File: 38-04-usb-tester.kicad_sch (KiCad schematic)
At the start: 64 parts, among them J1 USB3_A_HC-USB3.0-L168-WP, J2 USB_Micro-B_KH-MICRO5P-JN, J3 USB_C_12401832E402A, J4 USB_Mini-B_U-M-M5DD-W-1, J5 Conn_01x05_Pin, J6 USB_C_12401832E402A, SW1 SW_SPDT, U1 STM32C031K6Tx

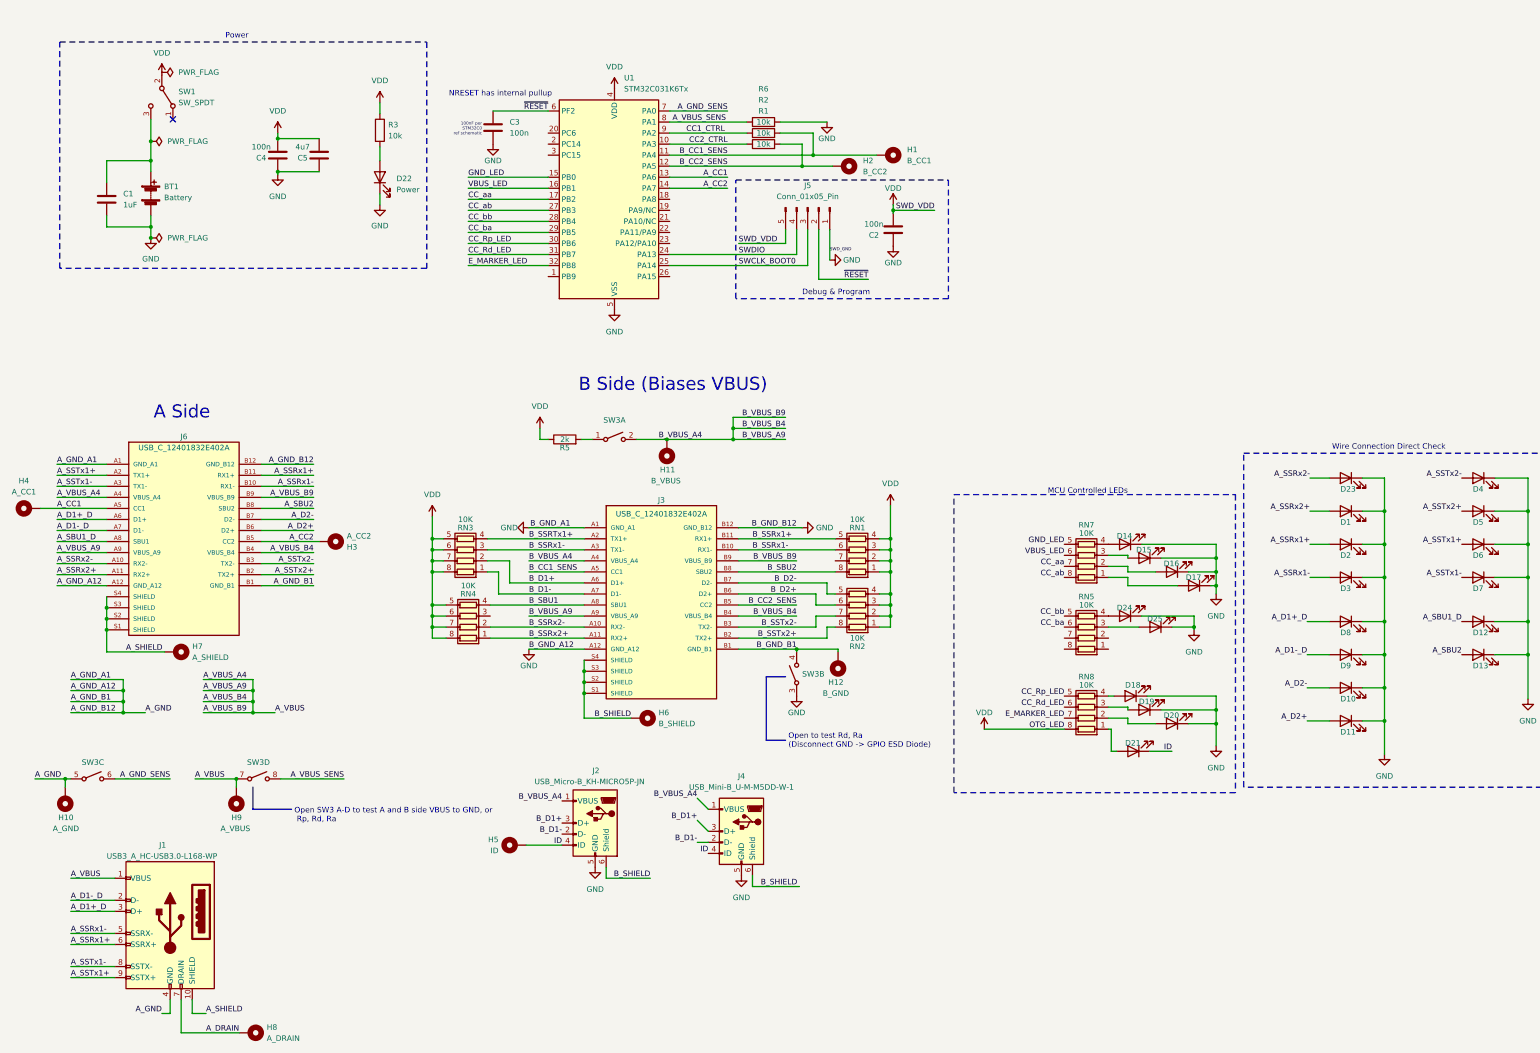
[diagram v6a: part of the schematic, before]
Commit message: edge pads and start of pcb layout
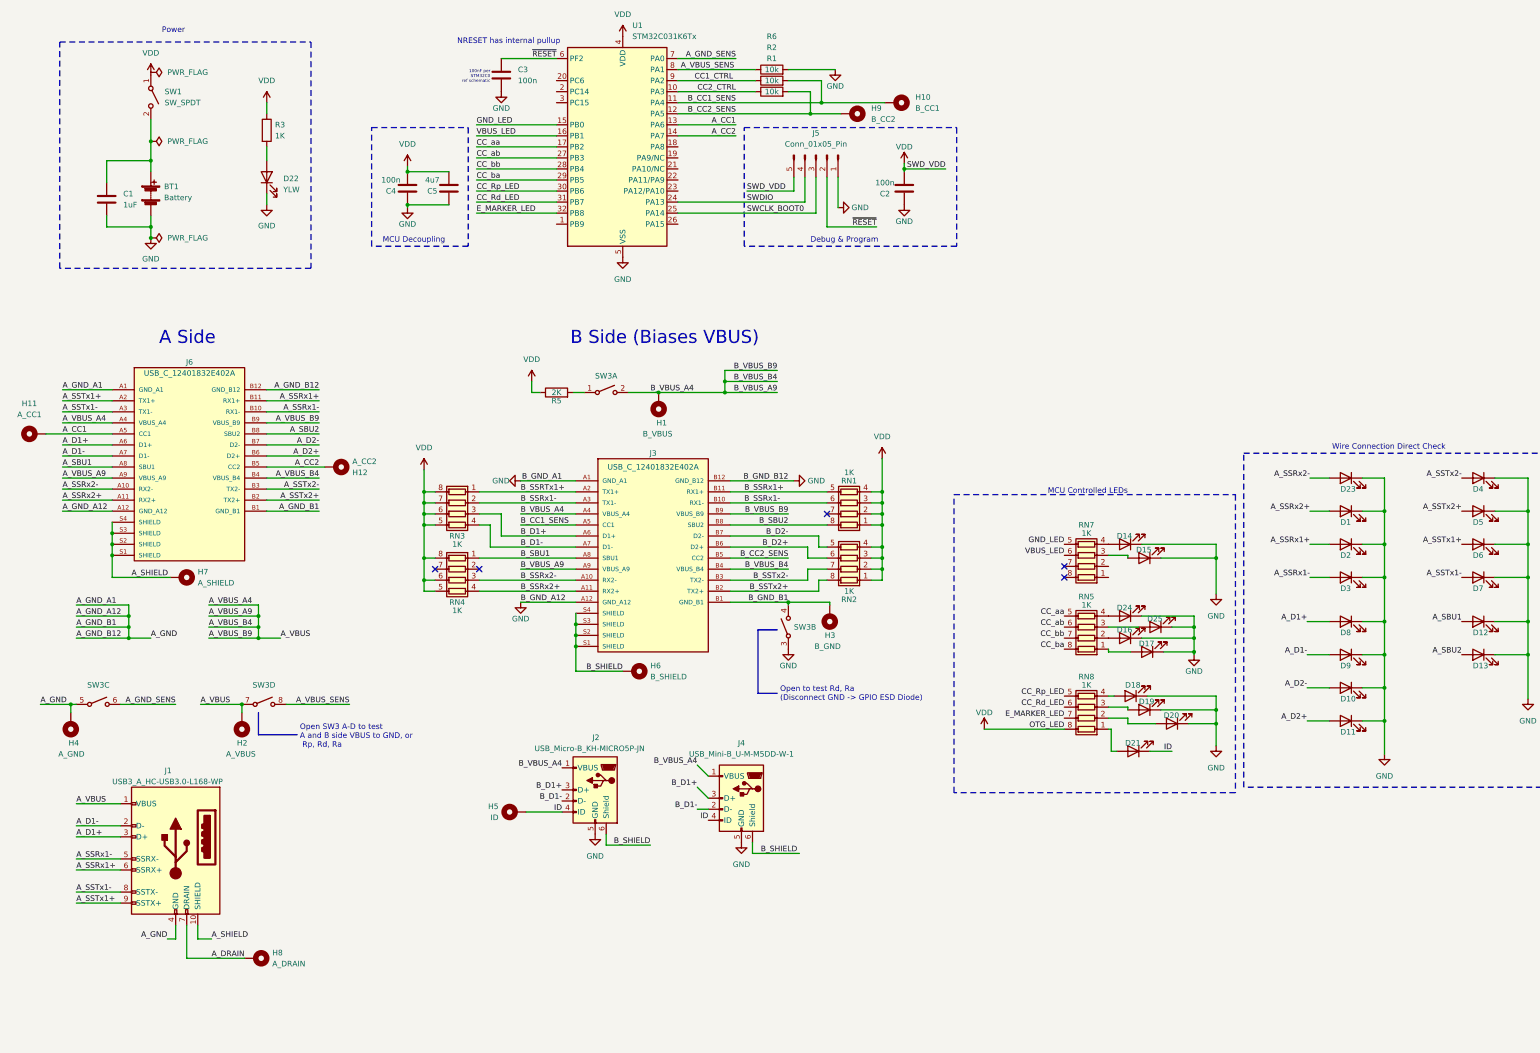
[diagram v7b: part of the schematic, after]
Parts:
- BT1: footprint Battery:BatteryHolder_Keystone_1058_1x2032 -> Battery:BatteryHolder_Keystone_103_1x20mm
- C1, C2, C3, C4, C5: footprint Capacitor_SMD:C_0805_2012Metric -> Capacitor_SMD:C_0603_1608Metric
- D1, D13, D9: value SSRx2+_D -> YLW; JLPCB_MPN (none) -> 17-21UYC/S530-A3/TR8; JLPCB_Mfg (none) -> Everlight Elec; JLPCB_Part_No (none) -> C91839; JLPCB_Price (none) -> $0.0218; JLPCB_URL (none) -> https://jlcpcb.com/parts/2nd/Optocoupler_LED_Digital_Tube_P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
- D10, D2: value SSRx1+_D -> YLW; JLPCB_MPN (none) -> 17-21UYC/S530-A3/TR8; JLPCB_Mfg (none) -> Everlight Elec; JLPCB_Part_No (none) -> C91839; JLPCB_Price (none) -> $0.0218; JLPCB_URL (none) -> https://jlcpcb.com/parts/2nd/Optocoupler_LED_Digital_Tube_P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
- D11, D3: value SSRx1-_D -> YLW; JLPCB_MPN (none) -> 17-21UYC/S530-A3/TR8; JLPCB_Mfg (none) -> Everlight Elec; JLPCB_Part_No (none) -> C91839; JLPCB_Price (none) -> $0.0218; JLPCB_URL (none) -> https://jlcpcb.com/parts/2nd/Optocoupler_LED_Digital_Tube_P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
- D12, D23, D8: value SSRx2-_D -> YLW; JLPCB_MPN (none) -> 17-21UYC/S530-A3/TR8; JLPCB_Mfg (none) -> Everlight Elec; JLPCB_Part_No (none) -> C91839; JLPCB_Price (none) -> $0.0218; JLPCB_URL (none) -> https://jlcpcb.com/parts/2nd/Optocoupler_LED_Digital_Tube_P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
- D14: value GND_D -> YLW; JLPCB_MPN (none) -> 17-21UYC/S530-A3/TR8; JLPCB_Mfg (none) -> Everlight Elec; JLPCB_Part_No (none) -> C91839; JLPCB_Price (none) -> $0.0218; JLPCB_URL (none) -> https://jlcpcb.com/parts/2nd/Optocoupler_LED_Digital_Tube_P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
- D15: value VBUS_LED_D -> YLW; JLPCB_MPN (none) -> 17-21UYC/S530-A3/TR8; JLPCB_Mfg (none) -> Everlight Elec; JLPCB_Part_No (none) -> C91839; JLPCB_Price (none) -> $0.0218; JLPCB_URL (none) -> https://jlcpcb.com/parts/2nd/Optocoupler_LED_Digital_Tube_P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
- D16: value CC_NORM_D -> YLW; JLPCB_MPN (none) -> 17-21UYC/S530-A3/TR8; JLPCB_Mfg (none) -> Everlight Elec; JLPCB_Part_No (none) -> C91839; JLPCB_Price (none) -> $0.0218; JLPCB_URL (none) -> https://jlcpcb.com/parts/2nd/Optocoupler_LED_Digital_Tube_P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
- D17: value CC_REV_D -> YLW; JLPCB_MPN (none) -> 17-21UYC/S530-A3/TR8; JLPCB_Mfg (none) -> Everlight Elec; JLPCB_Part_No (none) -> C91839; JLPCB_Price (none) -> $0.0218; JLPCB_URL (none) -> https://jlcpcb.com/parts/2nd/Optocoupler_LED_Digital_Tube_P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
- D18: value Rp_D -> YLW; JLPCB_MPN (none) -> 17-21UYC/S530-A3/TR8; JLPCB_Mfg (none) -> Everlight Elec; JLPCB_Part_No (none) -> C91839; JLPCB_Price (none) -> $0.0218; JLPCB_URL (none) -> https://jlcpcb.com/parts/2nd/Optocoupler_LED_Digital_Tube_P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
- D19: value Rd_D -> YLW; JLPCB_MPN (none) -> 17-21UYC/S530-A3/TR8; JLPCB_Mfg (none) -> Everlight Elec; JLPCB_Part_No (none) -> C91839; JLPCB_Price (none) -> $0.0218; JLPCB_URL (none) -> https://jlcpcb.com/parts/2nd/Optocoupler_LED_Digital_Tube_P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
- D20: value Ra_D -> YLW; JLPCB_MPN (none) -> 17-21UYC/S530-A3/TR8; JLPCB_Mfg (none) -> Everlight Elec; JLPCB_Part_No (none) -> C91839; JLPCB_Price (none) -> $0.0218; JLPCB_URL (none) -> https://jlcpcb.com/parts/2nd/Optocoupler_LED_Digital_Tube_P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
- D21: value OTG_D -> YLW; JLPCB_MPN (none) -> 17-21UYC/S530-A3/TR8; JLPCB_Mfg (none) -> Everlight Elec; JLPCB_Part_No (none) -> C91839; JLPCB_Price (none) -> $0.0218; JLPCB_URL (none) -> https://jlcpcb.com/parts/2nd/Optocoupler_LED_Digital_Tube_P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
- D22: value Power -> YLW; JLPCB_MPN (none) -> 17-21UYC/S530-A3/TR8; JLPCB_Mfg (none) -> Everlight Elec; JLPCB_Part_No (none) -> C91839; JLPCB_Price (none) -> $0.0218; JLPCB_URL (none) -> https://jlcpcb.com/parts/2nd/Optocoupler_LED_Digital_Tube_P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
- D24: value CC_bb_D -> YLW; JLPCB_MPN (none) -> 17-21UYC/S530-A3/TR8; JLPCB_Mfg (none) -> Everlight Elec; JLPCB_Part_No (none) -> C91839; JLPCB_Price (none) -> $0.0218; JLPCB_URL (none) -> https://jlcpcb.com/parts/2nd/Optocoupler_LED_Digital_Tube_P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
- D25: value CC_ba_D -> YLW; JLPCB_MPN (none) -> 17-21UYC/S530-A3/TR8; JLPCB_Mfg (none) -> Everlight Elec; JLPCB_Part_No (none) -> C91839; JLPCB_Price (none) -> $0.0218; JLPCB_URL (none) -> https://jlcpcb.com/parts/2nd/Optocoupler_LED_Digital_Tube_P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
- D4: value SSTx2-_D -> YLW; JLPCB_MPN (none) -> 17-21UYC/S530-A3/TR8; JLPCB_Mfg (none) -> Everlight Elec; JLPCB_Part_No (none) -> C91839; JLPCB_Price (none) -> $0.0218; JLPCB_URL (none) -> https://jlcpcb.com/parts/2nd/Optocoupler_LED_Digital_Tube_P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
- D5: value SSTx2+_D -> YLW; JLPCB_MPN (none) -> 17-21UYC/S530-A3/TR8; JLPCB_Mfg (none) -> Everlight Elec; JLPCB_Part_No (none) -> C91839; JLPCB_Price (none) -> $0.0218; JLPCB_URL (none) -> https://jlcpcb.com/parts/2nd/Optocoupler_LED_Digital_Tube_P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
- D6: value SSTx1+_D -> YLW; JLPCB_MPN (none) -> 17-21UYC/S530-A3/TR8; JLPCB_Mfg (none) -> Everlight Elec; JLPCB_Part_No (none) -> C91839; JLPCB_Price (none) -> $0.0218; JLPCB_URL (none) -> https://jlcpcb.com/parts/2nd/Optocoupler_LED_Digital_Tube_P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
- D7: value SSTx1-_D -> YLW; JLPCB_MPN (none) -> 17-21UYC/S530-A3/TR8; JLPCB_Mfg (none) -> Everlight Elec; JLPCB_Part_No (none) -> C91839; JLPCB_Price (none) -> $0.0218; JLPCB_URL (none) -> https://jlcpcb.com/parts/2nd/Optocoupler_LED_Digital_Tube_P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
- H1: renamed from H11; footprint MountingHole:MountingHole_2.5mm_Pad_TopBottom -> 01-UserLibary:Connector_Pad_Edge_Oval_5mm_Extended; JLPCB_MPN (none) -> x
- H10: renamed from H1; footprint MountingHole:MountingHole_2.5mm_Pad_TopBottom -> 01-UserLibary:Connector_Pad_Edge_Oval_5mm_Extended; JLPCB_MPN (none) -> x
- H11: renamed from H4; footprint MountingHole:MountingHole_2.5mm_Pad_TopBottom -> 01-UserLibary:Connector_Pad_Edge_Oval_5mm_Extended; JLPCB_MPN (none) -> x
- H12: renamed from H3; footprint MountingHole:MountingHole_2.5mm_Pad_TopBottom -> 01-UserLibary:Connector_Pad_Edge_Oval_5mm_Extended; JLPCB_MPN (none) -> x
- H2: renamed from H9; footprint MountingHole:MountingHole_2.5mm_Pad_TopBottom -> 01-UserLibary:Connector_Pad_Edge_Oval_5mm_Extended; JLPCB_MPN (none) -> x
- H3: renamed from H12; footprint MountingHole:MountingHole_2.5mm_Pad_TopBottom -> 01-UserLibary:Connector_Pad_Edge_Oval_5mm_Extended; JLPCB_MPN (none) -> x
- H4: renamed from H10; footprint MountingHole:MountingHole_2.5mm_Pad_TopBottom -> 01-UserLibary:Connector_Pad_Edge_Oval_5mm_Extended; JLPCB_MPN (none) -> x
- H5, H6, H7, H8: footprint MountingHole:MountingHole_2.5mm_Pad_TopBottom -> TestPoint:TestPoint_THTPad_D1.5mm_Drill0.7mm; JLPCB_MPN (none) -> x
- H9: renamed from H2; footprint MountingHole:MountingHole_2.5mm_Pad_TopBottom -> 01-UserLibary:Connector_Pad_Edge_Oval_5mm_Extended; JLPCB_MPN (none) -> x
- J5: JLPCB_MPN (none) -> x
- R3: value 10k -> 1K
- R5: value 2k -> 2K; footprint (none) -> Resistor_SMD:R_0201_0603Metric
- RN1, RN2, RN3, RN4, RN5, RN7, RN8: value 10K -> 1K; JLPCB_MPN (none) -> YC164-JR-071K1L; JLPCB_Mfg (none) -> YAGEO; JLPCB_Part_No (none) -> C136833; JLPCB_Price (none) -> $0.007; JLPCB_URL (none) -> https://jlcpcb.com/parts/2nd/Resistors/Resistor_Networks_Ar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
- SW1: footprint (none) -> Button_Switch_SMD:SW_DIP_SPSTx01_Slide_6.7x4.1mm_W8.61mm_P2.54mm_LowProfile; symbol Switch:SW_SPDT -> Switch:SW_SPST
- SW3: value ~ -> ZX-1.27BM-4PSMD
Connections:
- net B_D1+: now also RN3.3 (R3.1); no longer RN3.2 (R2.1)
- net B_D1-: now also RN3.4 (R4.1); no longer RN3.1 (R1.1)
- net B_SBU1: now also RN4.1 (R1.1); no longer RN4.4 (R4.1)
- net B_SSRTx1+: now also RN3.1 (R1.1); no longer RN3.4 (R4.1)
- net B_SSRx1-: now also RN3.2 (R2.1); no longer RN3.3 (R3.1)
- net B_SSRx2+: now also RN4.4 (R4.1); no longer RN4.1 (R1.1)
- net B_SSRx2-: now also RN4.3 (R3.1); no longer RN4.2 (R2.1)
- net CC_aa: now also RN5.5 (R4.2); no longer RN7.7 (R2.2)
- net CC_ab: now also RN5.6 (R3.2); no longer RN7.8 (R1.2)
- net CC_ba: now also RN5.8 (R1.2); no longer RN5.6 (R3.2)
- net CC_bb: now also RN5.7 (R2.2); no longer RN5.5 (R4.2)
- net VCC: now also SW1.1 (A); no longer RN4.7 (R2.2), SW1.2 (B)
- net at D16.2 (A): now also RN5.2 (R2.1); no longer RN7.2 (R2.1)
- net at BT1.1 (+), C1.1: now also SW1.2 (B); no longer SW1.3 (C)
- net at D17.2 (A): now also RN5.1 (R1.1); no longer RN7.1 (R1.1)
- net A_D1+_D renamed A_D1+
- net A_D1-_D renamed A_D1-
- net A_SBU1_D renamed A_SBU1
- no-connect marks 1 -> 5
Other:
- note added: "MCU Decoupling"
- moved on the sheet: C2, C3, C4, C5, D22, H1, H10, H11, H12, H2, H3, H4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

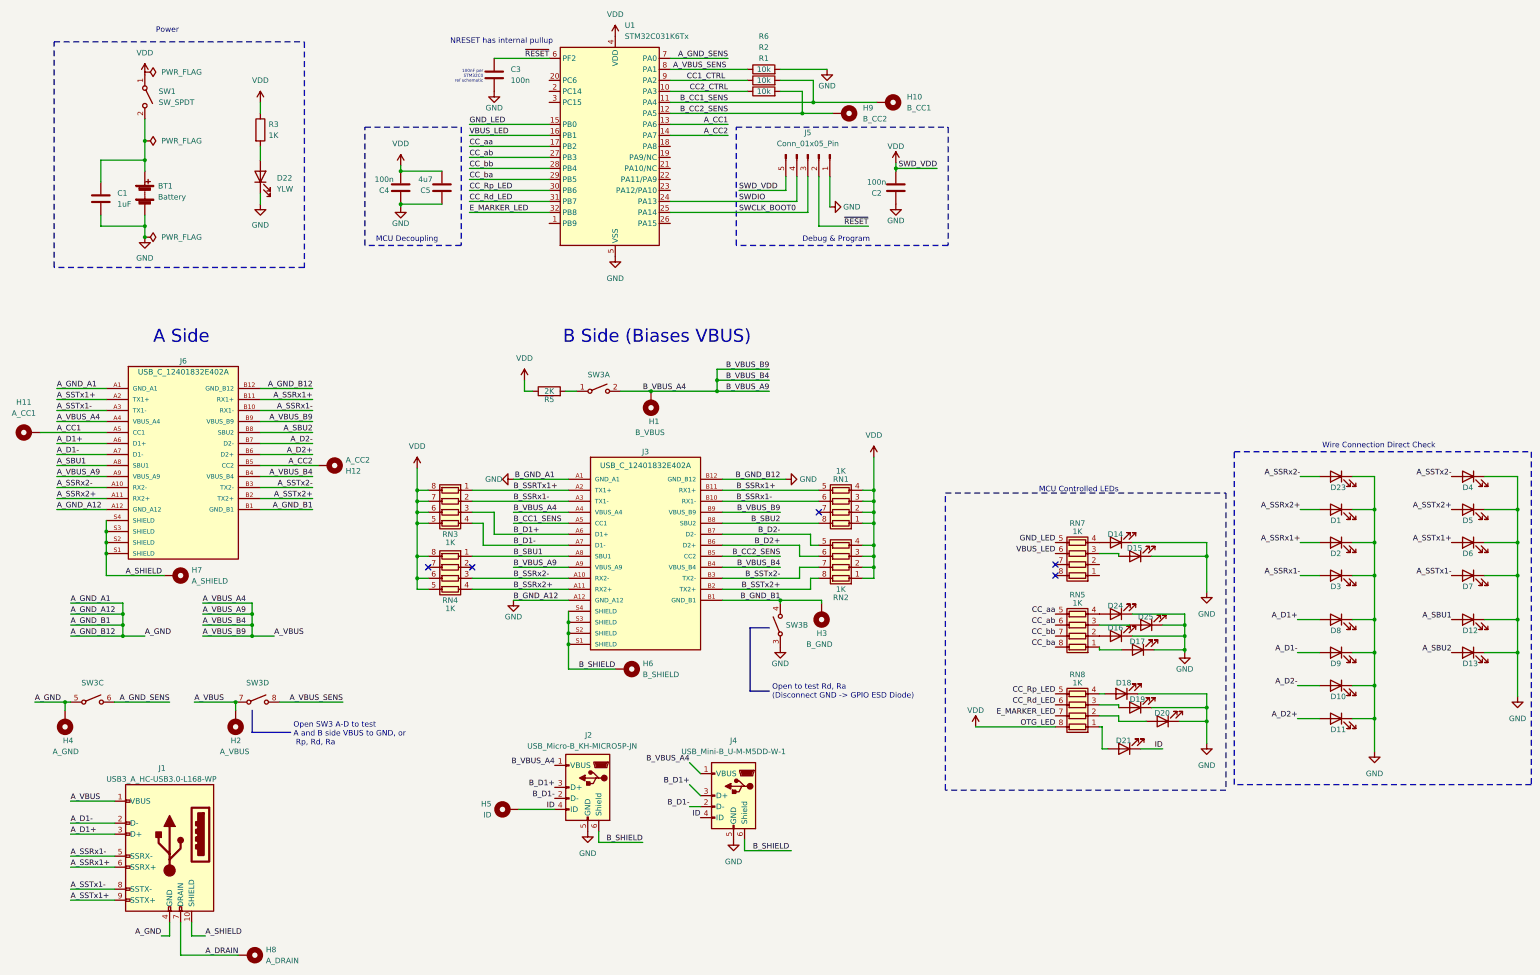
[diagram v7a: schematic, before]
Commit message: pcb layout - cleanup, DNP decisions
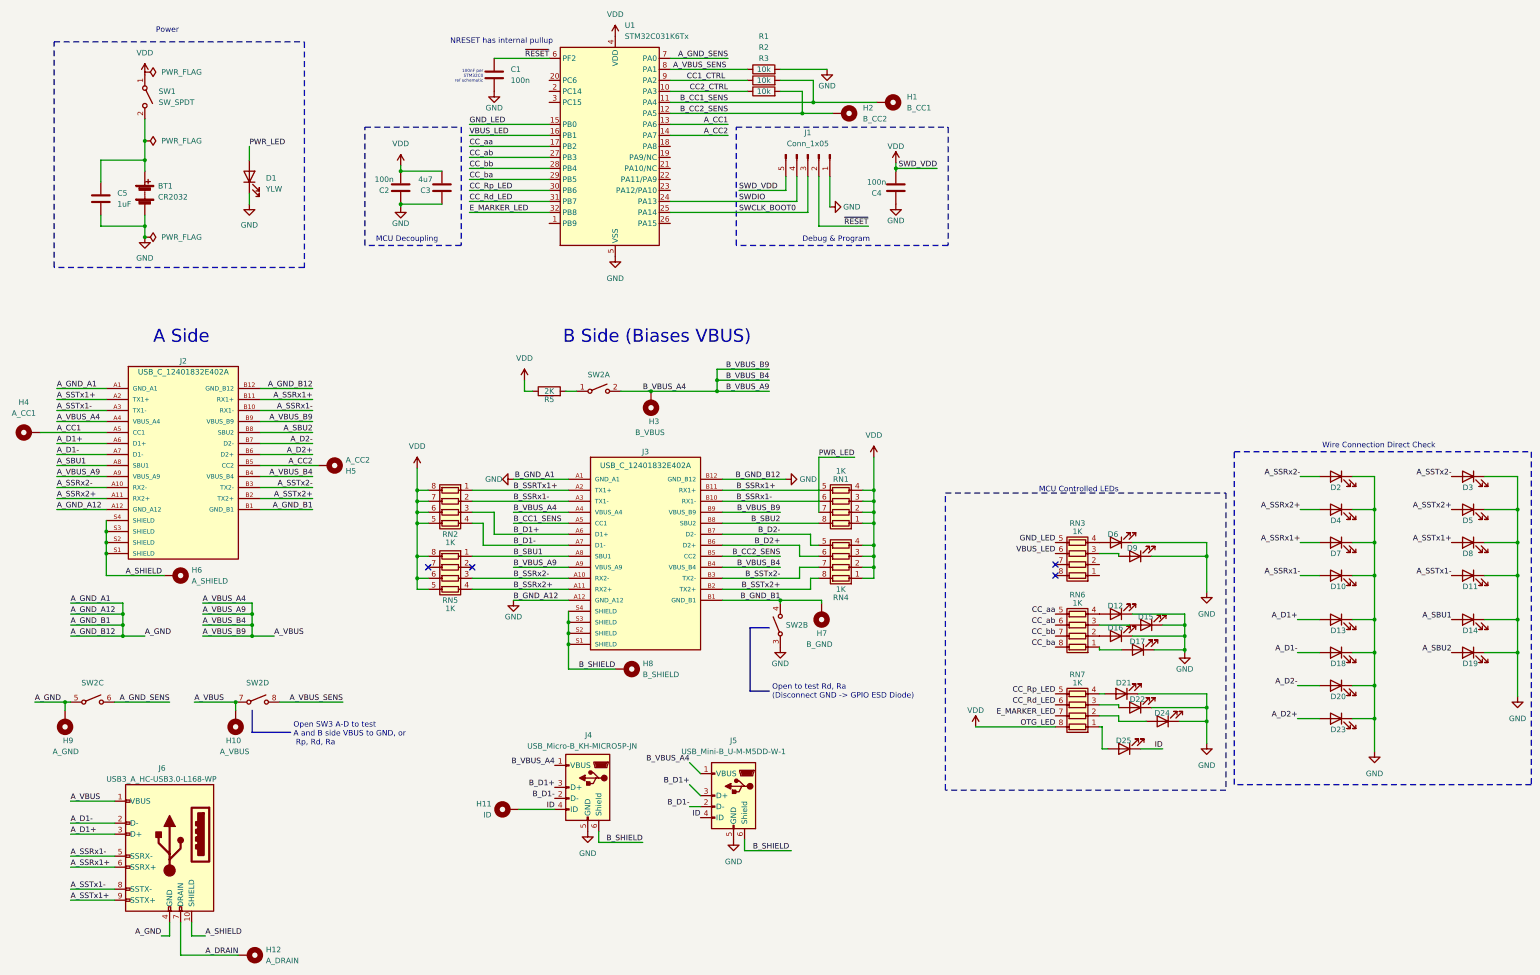
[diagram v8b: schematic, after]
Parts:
- removed R3: 1K, Resistor_SMD:R_0201_0603Metric, symbol Device:R
- BT1: value Battery -> CR2032; JLPCB_MPN (none) -> DNP; JLPCB_Mfg (none) -> DNP; JLPCB_Part_No (none) -> DNP; JLPCB_Price (none) -> DNP
- C1: renamed from C3; footprint Capacitor_SMD:C_0603_1608Metric -> Capacitor_SMD:C_0402_1005Metric; JLPCB_MPN (none) -> CC0402MRY5V6BB104; JLPCB_Mfg (none) -> YAGEO; JLPCB_Part_No (none) -> C527030; JLPCB_Price (none) -> $0.0016
- C2: renamed from C4; footprint Capacitor_SMD:C_0603_1608Metric -> Capacitor_SMD:C_0402_1005Metric; JLPCB_MPN (none) -> CC0402MRY5V6BB104; JLPCB_Mfg (none) -> YAGEO; JLPCB_Part_No (none) -> C527030; JLPCB_Price (none) -> $0.0016
- C3: renamed from C5; footprint Capacitor_SMD:C_0603_1608Metric -> Capacitor_SMD:C_0805_2012Metric_Pad1.18x1.45mm_HandSolder; JLPCB_MPN (none) -> DNP; JLPCB_Mfg (none) -> DNP; JLPCB_Part_No (none) -> DNP; JLPCB_Price (none) -> DNP
- C4: renamed from C2; footprint Capacitor_SMD:C_0603_1608Metric -> Capacitor_SMD:C_0402_1005Metric; JLPCB_MPN (none) -> CC0402MRY5V6BB104; JLPCB_Mfg (none) -> YAGEO; JLPCB_Part_No (none) -> C527030; JLPCB_Price (none) -> $0.0016
- C5: renamed from C1; footprint Capacitor_SMD:C_0603_1608Metric -> Capacitor_SMD:C_0805_2012Metric_Pad1.18x1.45mm_HandSolder; JLPCB_MPN (none) -> DNP; JLPCB_Mfg (none) -> DNP; JLPCB_Part_No (none) -> DNP; JLPCB_Price (none) -> DNP
- H1: renamed from H10; JLPCB_Mfg (none) -> x; JLPCB_Part_No (none) -> x; JLPCB_Price (none) -> x
- H10: renamed from H2; JLPCB_Mfg (none) -> x; JLPCB_Part_No (none) -> x; JLPCB_Price (none) -> x
- H11: renamed from H5; JLPCB_Mfg (none) -> x; JLPCB_Part_No (none) -> x; JLPCB_Price (none) -> x
- H12: renamed from H8; JLPCB_Mfg (none) -> x; JLPCB_Part_No (none) -> x; JLPCB_Price (none) -> x
- H2: renamed from H9; JLPCB_Mfg (none) -> x; JLPCB_Part_No (none) -> x; JLPCB_Price (none) -> x
- H3: renamed from H1; JLPCB_Mfg (none) -> x; JLPCB_Part_No (none) -> x; JLPCB_Price (none) -> x
- H4: renamed from H11; JLPCB_Mfg (none) -> x; JLPCB_Part_No (none) -> x; JLPCB_Price (none) -> x
- H5: renamed from H12; JLPCB_Mfg (none) -> x; JLPCB_Part_No (none) -> x; JLPCB_Price (none) -> x
- H6: renamed from H7; JLPCB_Mfg (none) -> x; JLPCB_Part_No (none) -> x; JLPCB_Price (none) -> x
- H7: renamed from H3; JLPCB_Mfg (none) -> x; JLPCB_Part_No (none) -> x; JLPCB_Price (none) -> x
- H8: renamed from H6; JLPCB_Mfg (none) -> x; JLPCB_Part_No (none) -> x; JLPCB_Price (none) -> x
- H9: renamed from H4; JLPCB_Mfg (none) -> x; JLPCB_Part_No (none) -> x; JLPCB_Price (none) -> x
- J1: renamed from J5; value Conn_01x05_Pin -> Conn_1x05; JLPCB_MPN x -> DNP; JLPCB_Mfg (none) -> DNP; JLPCB_Part_No (none) -> DNP; JLPCB_Price (none) -> DNP
- J6: renamed from J1; footprint 01-UserLibary:HC-USB3.0-L168-WP_USB-A_THT-9-2MP_P2.0mm -> 01-UserLibary:USB3_A_Hong-Cheng_HC-USB3.0-L168-WP_THT-9-2MP_P2.0mm
- R1: renamed from R6; JLPCB_MPN (none) -> 🔶TBD; JLPCB_Mfg (none) -> 🔶TBD; JLPCB_Part_No (none) -> 🔶TBD; JLPCB_Price (none) -> 🔶TBD
- R2: JLPCB_MPN (none) -> 🔶TBD; JLPCB_Mfg (none) -> 🔶TBD; JLPCB_Part_No (none) -> 🔶TBD; JLPCB_Price (none) -> 🔶TBD
- R3: renamed from R1; JLPCB_MPN (none) -> 🔶TBD; JLPCB_Mfg (none) -> 🔶TBD; JLPCB_Part_No (none) -> 🔶TBD; JLPCB_Price (none) -> 🔶TBD
- R5: JLPCB_MPN (none) -> DNP; JLPCB_Mfg (none) -> DNP; JLPCB_Part_No (none) -> DNP; JLPCB_Price (none) -> DNP
- SW1: JLPCB_MPN (none) -> 🔶TBD (footprint); JLPCB_Mfg (none) -> 🔶TBD; JLPCB_Part_No (none) -> 🔶TBD; JLPCB_Price (none) -> 🔶TBD
- SW2: renamed from SW3; JLPCB_MPN ZX-1.27BM-4PSMD -> ZX-1.27BM-4PSMD
- renumbered D22 to D1, D3 to D10, D7 to D11, D24 to D12, D8 to D13, D12 to D14, D25 to D15, D9 to D18, D13 to D19, D23 to D2, D10 to D20, D18 to D21, D19 to D22, D11 to D23, D20 to D24, D21 to D25, D4 to D3, D1 to D4, D14 to D6, D2 to D7, D6 to D8, D15 to D9, J6 to J2, J2 to J4, J4 to J5, RN3 to RN2, RN7 to RN3, RN2 to RN4, RN4 to RN5, RN5 to RN6, RN8 to RN7
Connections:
- net VCC: no longer U1.4 (VDD)
- net PWR_LED: now reaches RN1.7 (R2.2)
- net PWR_LED: now also D1.2 (A)
- new net VDD: U1.4 (VDD)
- no-connect marks 5 -> 4
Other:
- moved on the sheet: D1
